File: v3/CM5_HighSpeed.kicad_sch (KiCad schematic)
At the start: 6 parts, among them J2 Conn_01x22_Female, J3 Conn_01x22_Female

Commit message: Various pcb mods
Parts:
- removed Module1: ComputeModule5-CM5, CM5IO:Raspberry-Pi-5-Compute-Module, symbol CM5IO:ComputeModule5-CM5
- added J8: 10164227-1001A1RLF, CM5IO:CM5_connector, symbol cm5_b:CM5_b
- J2, J3: LCSC PN (none) -> C597981
- R2, R3, R4: Field6 (none) -> 0402WGF2201TCE; LCSC PN (none) -> C25879
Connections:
- net DPHY0_C_N: now also J8.27 (MIPI0_C_N)
- net DPHY0_C_P: now also J8.29 (MIPI0_C_P)
- net DPHY0_D0_N: now also J8.15 (MIPI0_D0_N)
- net DPHY0_D0_P: now also J8.17 (MIPI0_D0_P)
- net DPHY0_D1_N: now also J8.21 (MIPI0_D1_N)
- net DPHY0_D1_P: now also J8.23 (MIPI0_D1_P)
- net DPHY0_D2_N: now also J8.33 (MIPI0_D2_N)
- net DPHY0_D2_P: now also J8.35 (MIPI0_D2_P)
- net DPHY0_D3_N: now also J8.39 (MIPI0_D3_N)
- net DPHY0_D3_P: now also J8.41 (MIPI0_D3_P)
- net DPHY1_C_N: now also J8.87 (MIPI1_C_N)
- net DPHY1_C_P: now also J8.89 (MIPI1_C_P)
- net DPHY1_D0_N: now also J8.75 (MIPI1_D0_N)
- net DPHY1_D0_P: now also J8.77 (MIPI1_D0_P)
- net DPHY1_D1_N: now also J8.81 (MIPI1_D1_N)
- net DPHY1_D1_P: now also J8.83 (MIPI1_D1_P)
- net DPHY1_D2_N: now also J8.93 (MIPI1_D2_N)
- net DPHY1_D2_P: now also J8.95 (MIPI1_D2_P)
- net DPHY1_D3_N: now also J8.94 (MIPI1_D3_N)
- net DPHY1_D3_P: now also J8.96 (MIPI1_D3_P)
- net GND: now also J8.13 (GND), J8.14 (GND), J8.19 (GND), J8.20 (GND), J8.25 (GND), J8.26 (GND), J8.31 (GND), J8.32 (GND), J8.37 (GND), J8.38 (GND), J8.44 (GND), J8.50 (GND), J8.55 (GND), J8.56 (GND), J8.61 (GND), J8.62 (GND), J8.67 (GND), J8.68 (GND), J8.7 (GND), J8.73 (GND), J8.74 (GND), J8.79 (GND), J8.8 (GND), J8.80 (GND), J8.85 (GND), J8.86 (GND), J8.91 (GND), J8.92 (GND), J8.97 (GND), J8.98 (GND)
- net HDMI0_CEC: now also J8.51 (HDMI0_CEC)
- net HDMI0_CK_N: now also J8.90 (HDMI0_CLK_N)
- net HDMI0_CK_P: now also J8.88 (HDMI0_CLK_P)
- net HDMI0_D0_N: now also J8.84 (HDMI0_TX0_N)
- net HDMI0_D0_P: now also J8.82 (HDMI0_TX0_P)
- net HDMI0_D1_N: now also J8.78 (HDMI0_TX1_N)
- net HDMI0_D1_P: now also J8.76 (HDMI0_TX1_P)
- net HDMI0_D2_N: now also J8.72 (HDMI0_TX2_N)
- net HDMI0_D2_P: now also J8.70 (HDMI0_TX2_P)
- net HDMI0_HOTPLUG: now also J8.53 (HDMI0_HOTPLUG)
- net HDMI0_SCL: now also J8.100 (HDMI0_SCL)
- net HDMI0_SDA: now also J8.99 (HDMI0_SDA)
- net HDMI1_CEC: now also J8.49 (HDMI1_CEC)
- net HDMI1_CK_N: now also J8.66 (HDMI1_CLK_N)
- net HDMI1_CK_P: now also J8.64 (HDMI1_CLK_P)
- net HDMI1_D0_N: now also J8.60 (HDMI1_TX0_N)
- net HDMI1_D0_P: now also J8.58 (HDMI1_TX0_P)
- net HDMI1_D1_N: now also J8.54 (HDMI1_TX1_N)
- net HDMI1_D1_P: now also J8.52 (HDMI1_TX1_P)
- net HDMI1_D2_N: now also J8.48 (HDMI1_TX2_N)
- net HDMI1_D2_P: now also J8.46 (HDMI1_TX2_P)
- net HDMI1_HOTPLUG: now also J8.43 (HDMI1_HOTPLUG)
- net HDMI1_SCL: now also J8.47 (HDMI1_SCL)
- net HDMI1_SDA: now also J8.45 (HDMI1_SDA)
- net PCIE_CLK_N: now also J8.12 (PCIe_CLK_N)
- net PCIE_CLK_P: now also J8.10 (PCIe_CLK_P)
- net PCIE_PWR_EN: now also J8.6 (PCIE_PWR_EN)
- net PCIE_RX_N: now also J8.18 (PCIe_RX_N)
- net PCIE_RX_P: now also J8.16 (PCIe_RX_P)
- net PCIE_TX_N: now also J8.24 (PCIe_TX_N)
- net PCIE_TX_P: now also J8.22 (PCIe_TX_P)
- net PCIE_nCLKREQ: now also J8.2 (PCIe_nCLKREQ)
- net PCIE_nRST: now also J8.9 (PCIe_nRST)
- net PCIE_nWAKE: now also J8.4 (PCIE_nWAKE)
- net USB2_N: now also J8.3 (USB2_N)
- net USB2_P: now also J8.5 (USB2_P)
- net USB3-0-D_N: now also J8.36 (USB3-0-D_N)
- net USB3-0-D_P: now also J8.34 (USB3-0-D_P)
- net USB3-0-RX_N: now also J8.28 (USB3-0-RX_N)
- net USB3-0-RX_P: now also J8.30 (USB3-0-RX_P)
- net USB3-0-TX_N: now also J8.40 (USB3-0-TX_N)
- net USB3-0-TX_P: now also J8.42 (USB3-0-TX_P)
- net USB3-1-D_N: now also J8.65 (USB3-1-D_N)
- net USB3-1-D_P: now also J8.63 (USB3-1-D_P)
- net USB3-1-RX_N: now also J8.57 (USB3-1-RX_N)
- net USB3-1-RX_P: now also J8.59 (USB3-1-RX_P)
- net USB3-1-TX_N: now also J8.69 (USB3-1-TX_N)
- net USB3-1-TX_P: now also J8.71 (USB3-1-TX_P)
- net USBOTG_ID: now also J8.1 (USB_OTG_ID)
- net VBUS_EN: now also J8.11 (VBUS_EN)

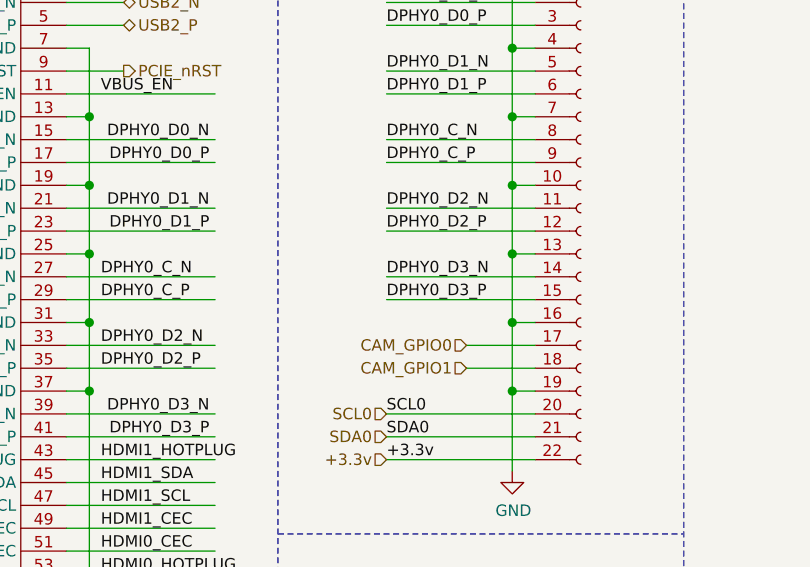
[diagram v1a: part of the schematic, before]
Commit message: convert to CS20 TOF
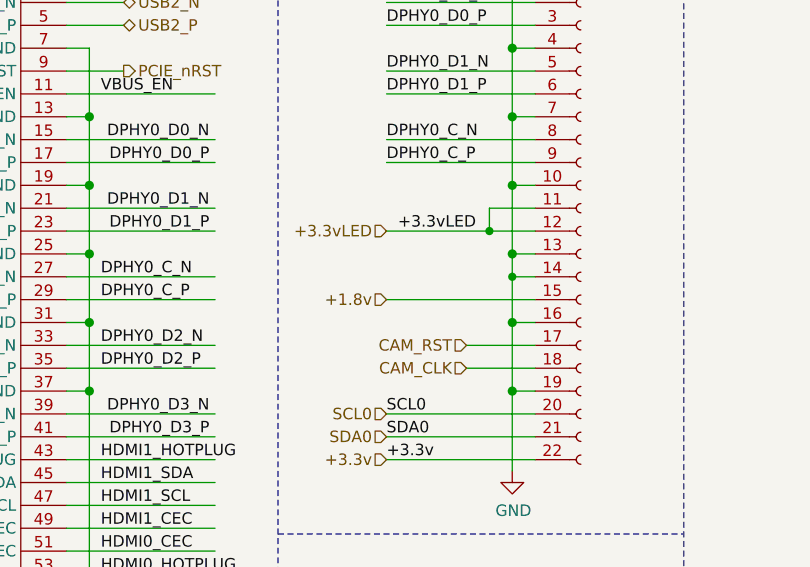
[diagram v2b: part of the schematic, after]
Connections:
- net DPHY0_D2_N: no longer J2.11 (Pin_11)
- net DPHY0_D2_P: no longer J2.12 (Pin_12)
- net DPHY0_D3_N: no longer J2.14 (Pin_14)
- net DPHY0_D3_P: no longer J2.15 (Pin_15)
- net GND: now also J2.14 (Pin_14)
- net CAM_GPIO0 renamed CAM_RST
- net CAM_GPIO1 renamed CAM_CLK
- new net +1.8v: J2.15 (Pin_15)
- new net +3.3vLED: J2.11 (Pin_11), J2.12 (Pin_12)
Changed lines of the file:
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@@
 	)
 	(junction
+		(at 146.05 53.34)
+		(diameter 0)
+		(color 0 0 0 0)
+	)
+	(junction
 		(at 101.6 147.32)
 		(diameter 1.016)
@@
 	)
 	(junction
+		(at 148.59 58.42)
+		(diameter 0)
+		(color 0 0 0 0)
+	)
+	(junction
 		(at 35.56 48.26)
 		(diameter 1.016)
@@
 	(wire
 		(pts
+			(xy 146.05 50.8) (xy 146.05 53.34)
+		)
+		(stroke
+			(width 0)
+			(type default)
+		)
+	)
+	(wire
+		(pts
 			(xy 35.56 33.02) (xy 35.56 40.64)
 		)
@@
 	(wire
 		(pts
-			(xy 148.59 55.88) (xy 148.59 63.5)
+			(xy 148.59 55.88) (xy 148.59 58.42)
 		)
 		(stroke
@@
 	(wire
 		(pts
+			(xy 148.59 58.42) (xy 151.13 58.42)
+		)
+		(stroke
+			(width 0)
+			(type solid)
+		)
+	)
+	(wire
+		(pts
 			(xy 21.59 127) (xy 38.1 127)
 		)
@@
 	(wire
 		(pts
+			(xy 151.13 50.8) (xy 146.05 50.8)
+		)
+		(stroke
+			(width 0)
+			(type default)
+		)
+	)
+	(wire
+		(pts
 			(xy 101.6 124.46) (xy 101.6 132.08)
 		)
@@
 	(wire
 		(pts
+			(xy 146.05 53.34) (xy 151.13 53.34)
+		)
+		(stroke
+			(width 0)
+			(type solid)
+		)
+	)
+	(wire
+		(pts
 			(xy 142.24 137.16) (xy 151.13 137.16)
 		)
@@
 	(wire
 		(pts
-			(xy 134.62 58.42) (xy 151.13 58.42)
-		)
-		(stroke
-			(width 0)
-			(type solid)
-		)
-	)
-	(wire
-		(pts
 			(xy 21.59 99.06) (xy 38.1 99.06)
 		)
@@
 	(wire
 		(pts
-			(xy 134.62 53.34) (xy 151.13 53.34)
+			(xy 134.62 53.34) (xy 146.05 53.34)
 		)
 		(stroke
@@
 	(wire
 		(pts
+			(xy 148.59 58.42) (xy 148.59 63.5)
+		)
+		(stroke
+			(width 0)
+			(type solid)
+		)
+	)
+	(wire
+		(pts
 			(xy 21.59 83.82) (xy 38.1 83.82)
 		)
@@
 	(wire
 		(pts
-			(xy 134.62 50.8) (xy 151.13 50.8)
-		)
-		(stroke
-			(width 0)
-			(type solid)
-		)
-	)
-	(wire
-		(pts
 			(xy 99.06 63.5) (xy 101.6 63.5)
 		)
@@
 		)
 	)
-	(label "DPHY0_D2_N"
-		(at 134.62 50.8 0)
+	(label "+3.3vLED"
+		(at 135.89 53.34 0)
 		(effects
 			(font
@@
 		)
 	)
-	(label "DPHY0_D2_P"
-		(at 134.62 53.34 0)
-		(effects
-			(font
-				(size 1.27 1.27)
-			)
-			(justify left bottom)
-		)
-	)
 	(label "DPHY0_D1_N"
 		(at 114.935 50.8 180)
@@
 		)
 	)
-	(label "DPHY0_D3_P"
-		(at 134.62 60.96 0)
-		(effects
-			(font
-				(size 1.27 1.27)
-			)
-			(justify left bottom)
-		)
-	)
 	(label "HDMI1_CK_P"
 		(at 21.59 104.14 0)
@@
 		)
 	)
-	(label "DPHY0_D3_N"
-		(at 134.62 58.42 0)
-		(effects
-			(font
-				(size 1.27 1.27)
-			)
-			(justify left bottom)
-		)
-	)
 	(label "USB3-1-RX_N"
 		(at 102.87 96.52 0)
@@
 		)
 	)
+	(hierarchical_label "+1.8v"
+		(shape input)
+		(at 134.62 60.96 180)
+		(effects
+			(font
+				(size 1.27 1.27)
+			)
+			(justify right)
+		)
+	)
 	(hierarchical_label "PCIE_PWR_EN"
 		(shape output)
@@
 		)
 	)
-	(hierarchical_label "CAM_GPIO0"
+	(hierarchical_label "CAM_RST"
 		(shape input)
 		(at 143.51 66.04 180)
@@
 		)
 	)
-	(hierarchical_label "CAM_GPIO1"
+	(hierarchical_label "CAM_CLK"
 		(shape input)
 		(at 143.51 68.58 180)
@@
 		(effects
 			(font
+				(size 1.27 1.27)
+			)
+			(justify right)
+		)
+	)
+	(hierarchical_label "+3.3vLED"
+		(shape input)
+		(at 134.62 53.34 180)
+		(effects
+			(font
